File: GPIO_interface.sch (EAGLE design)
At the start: 33 parts

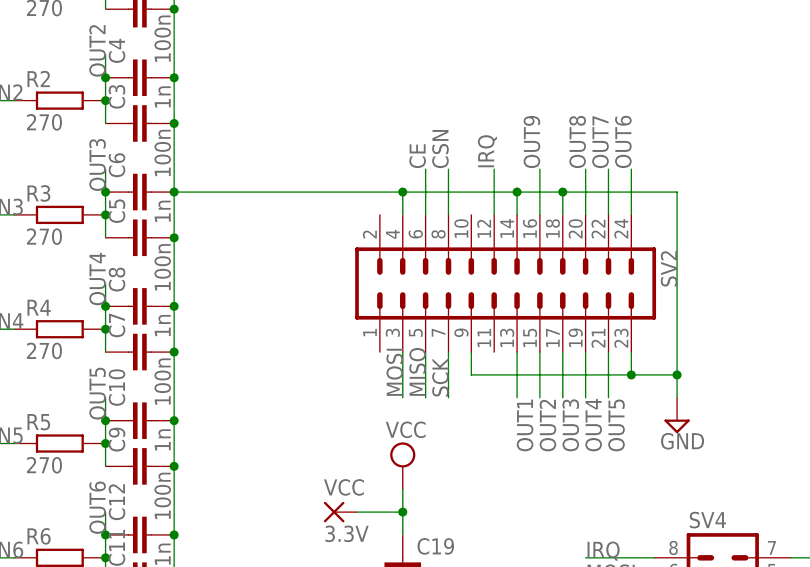
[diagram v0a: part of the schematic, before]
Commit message: wersja pod pcbs.io
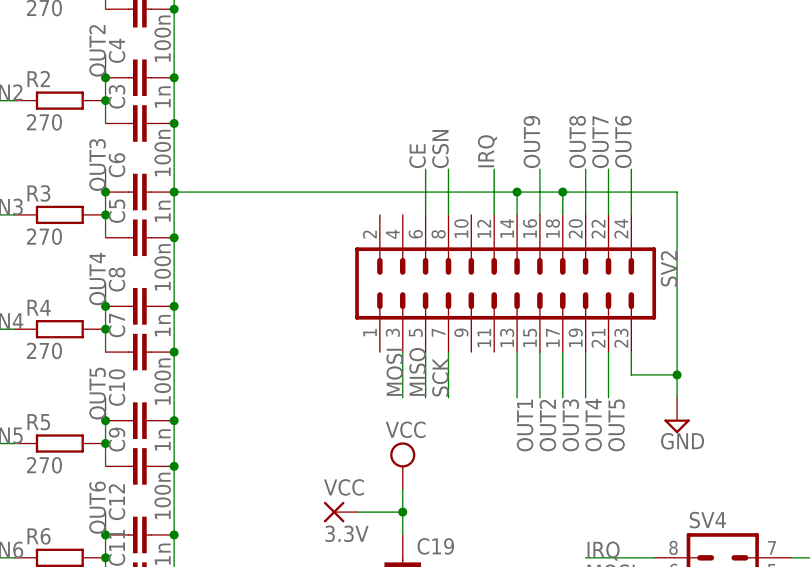
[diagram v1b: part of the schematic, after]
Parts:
- VCC: device wirepad:2,54/1,0 -> wirepad:1,6/0,9
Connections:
- net GND: no longer SV2.4, SV2.9
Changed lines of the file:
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@@
 <?xml version="1.0" encoding="utf-8"?>
 <!DOCTYPE eagle SYSTEM "eagle.dtd">
-<eagle version="6.5.0">
+<eagle version="6.6.0">
 <drawing>
 <settings>
@@
 <part name="SUPPLY6" library="supply2" deviceset="VCC" device=""/>
 <part name="SUPPLY7" library="supply2" deviceset="GND" device=""/>
-<part name="VCC" library="wirepad" deviceset="2,54/1,0" device="" value="3.3V"/>
+<part name="VCC" library="wirepad" deviceset="1,6/0,9" device="" value="3.3V"/>
 </parts>
 <sheets>
@@
 <instance part="SUPPLY6" gate="G$1" x="104.14" y="15.24" rot="R90"/>
 <instance part="SUPPLY7" gate="GND" x="132.08" y="15.24" rot="R90"/>
-<instance part="VCC" gate="P" x="73.66" y="27.94"/>
+<instance part="VCC" gate="1" x="73.66" y="27.94"/>
 </instances>
 <busses>
@@
 <pinref part="C17" gate="G$1" pin="2"/>
 <wire x1="55.88" y1="-12.7" x2="55.88" y2="-17.78" width="0.1524" layer="91"/>
-<wire x1="93.98" y1="63.5" x2="81.28" y2="63.5" width="0.1524" layer="91"/>
 <pinref part="SUPPLY1" gate="GND" pin="GND"/>
-<wire x1="81.28" y1="63.5" x2="55.88" y2="63.5" width="0.1524" layer="91"/>
+<wire x1="93.98" y1="63.5" x2="55.88" y2="63.5" width="0.1524" layer="91"/>
 <wire x1="111.76" y1="40.64" x2="111.76" y2="43.18" width="0.1524" layer="91"/>
 <junction x="55.88" y="-12.7"/>
@@
 <pinref part="SV2" gate="1" pin="18"/>
 <pinref part="SV2" gate="1" pin="23"/>
-<pinref part="SV2" gate="1" pin="9"/>
-<wire x1="88.9" y1="45.72" x2="88.9" y2="43.18" width="0.1524" layer="91"/>
-<wire x1="88.9" y1="43.18" x2="106.68" y2="43.18" width="0.1524" layer="91"/>
-<junction x="106.68" y="43.18"/>
-<pinref part="SV2" gate="1" pin="4"/>
-<wire x1="81.28" y1="60.96" x2="81.28" y2="63.5" width="0.1524" layer="91"/>
-<junction x="81.28" y="63.5"/>
 </segment>
 <segment>
@@
 <pinref part="C19" gate="G$1" pin="1"/>
 <wire x1="81.28" y1="30.48" x2="81.28" y2="27.94" width="0.1524" layer="91"/>
-<pinref part="VCC" gate="P" pin="P"/>
 <wire x1="81.28" y1="27.94" x2="81.28" y2="25.4" width="0.1524" layer="91"/>
 <wire x1="76.2" y1="27.94" x2="81.28" y2="27.94" width="0.1524" layer="91"/>
 <junction x="81.28" y="27.94"/>
-</segment>
-<segment>
+<pinref part="VCC" gate="1" pin="P"/>
+</segment>
+<segment>

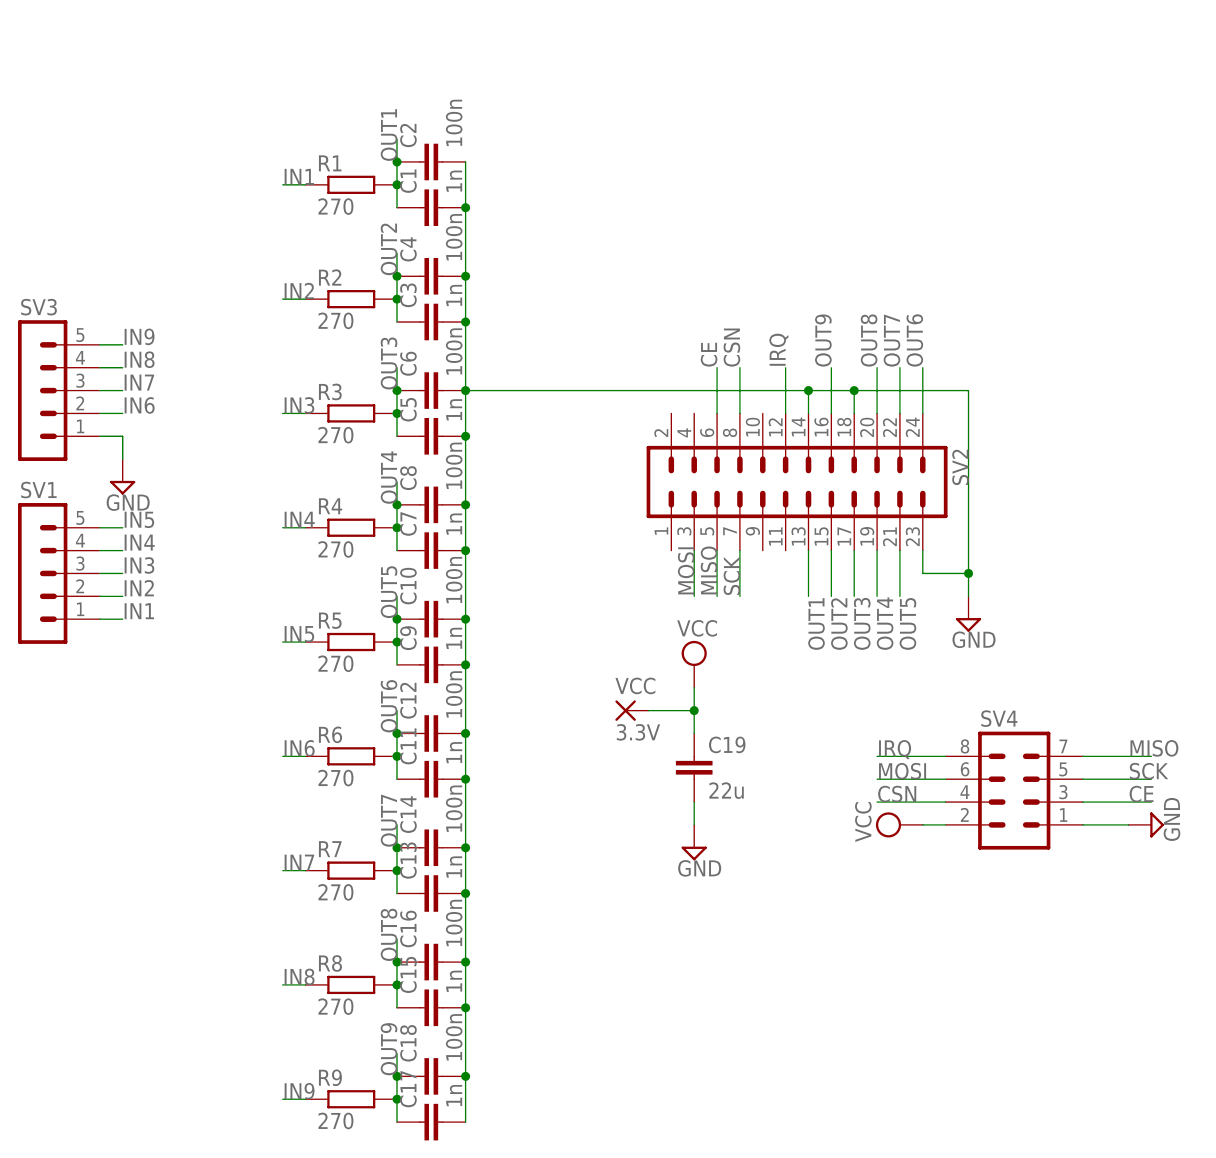
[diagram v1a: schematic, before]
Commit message: add LDO, use whole RPI connector
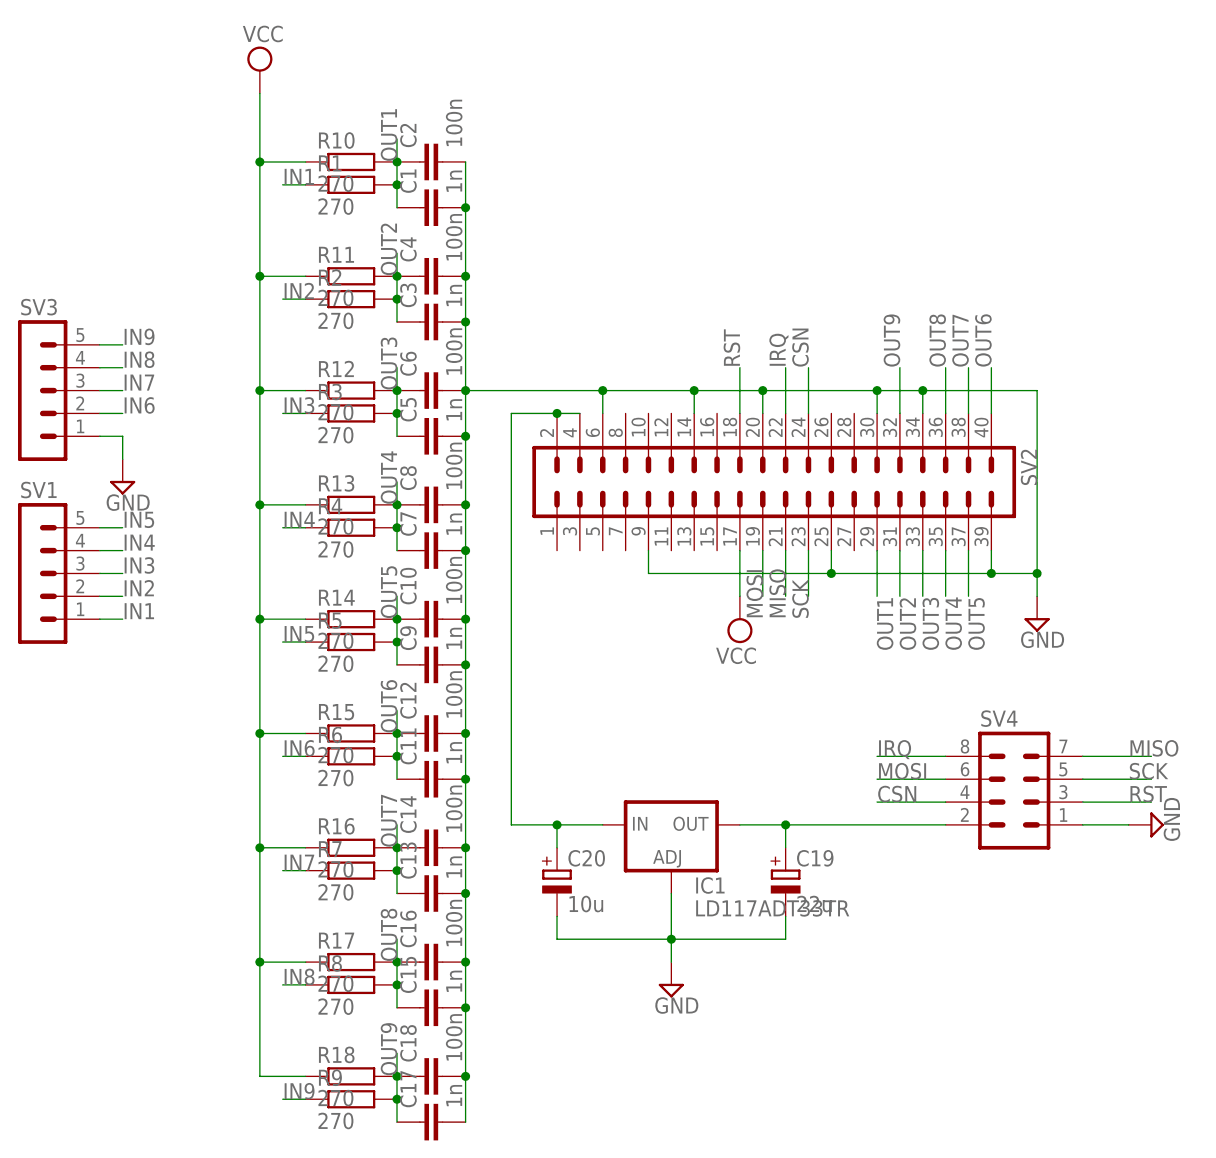
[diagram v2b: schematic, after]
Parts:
- removed VCC: 3.3V, wirepad:1,6/0,9
- added C20: 10u, rcl:CPOL-EUC/6032-28R
- added IC1: LD117ADT33TR, v-reg:LD117ADT33TR
- added R10, R11, R12, R13, R14, R15, R16, R17, R18: 270, rcl:R-EU_R0603
- C19: device rcl:C-EUC1206 -> rcl:CPOL-EUC/6032-28R
- SV2: device con-lstb:MA12-2 -> con-lstb:MA20-2
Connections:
- removed net CE: SV2.6, SV4.3
- new net N$1: C20.+, IC1.IN, SV2.2, SV2.4
- new net N$2: C19.+, IC1.OUT, SV4.2
- new net RST: SV2.18, SV4.3
- net CSN: now also SV2.24; no longer SV2.8
- net GND: now also C19.-, C20.-, IC1.ADJ, SV2.20, SV2.25, SV2.30, SV2.34, SV2.39, SV2.6, SV2.9; no longer C19.2, SV2.18, SV2.23
- net IRQ: now also SV2.22; no longer SV2.12
- net MISO: now also SV2.21; no longer SV2.5
- net MOSI: now also SV2.19; no longer SV2.3
- net OUT1: now also R10.2, SV2.29; no longer SV2.13
- net OUT2: now also R11.2, SV2.31; no longer SV2.15
- net OUT3: now also R12.2, SV2.33; no longer SV2.17
- net OUT4: now also R13.2, SV2.35; no longer SV2.19
- net OUT5: now also R14.2, SV2.37; no longer SV2.21
- net OUT6: now also R15.2, SV2.40; no longer SV2.24
- net OUT7: now also R16.2, SV2.38; no longer SV2.22
- net OUT8: now also R17.2, SV2.36; no longer SV2.20
- net OUT9: now also R18.2, SV2.32; no longer SV2.16
- net SCK: now also SV2.23; no longer SV2.7
- net VCC: now also R10.1, R11.1, R12.1, R13.1, R14.1, R15.1, R16.1, R17.1, R18.1, SV2.17; no longer C19.1, SV4.2, VCC.P

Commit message: cleanup names on pcb
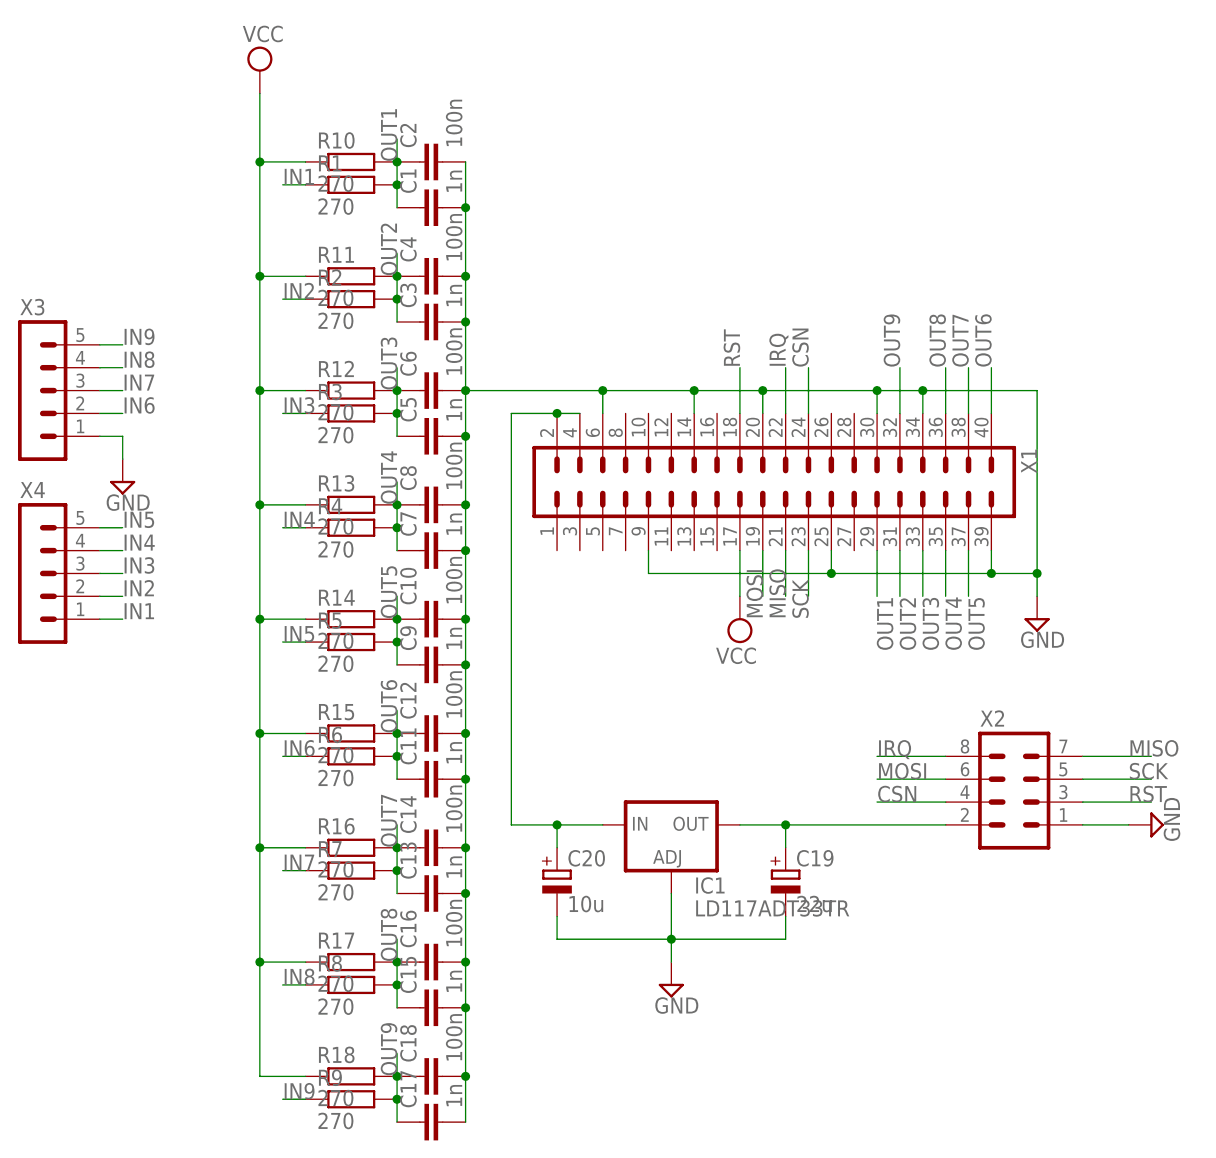
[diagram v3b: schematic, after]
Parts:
- renumbered SV1 to X4, SV2 to X1, SV3 to X3, SV4 to X2
